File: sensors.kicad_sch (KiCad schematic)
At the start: 24 parts, among them J10 PH-2P, J11 PH-2P, J12 PH-2P, J13 PH-2P, J14 PH-2P, J15 PH-3P

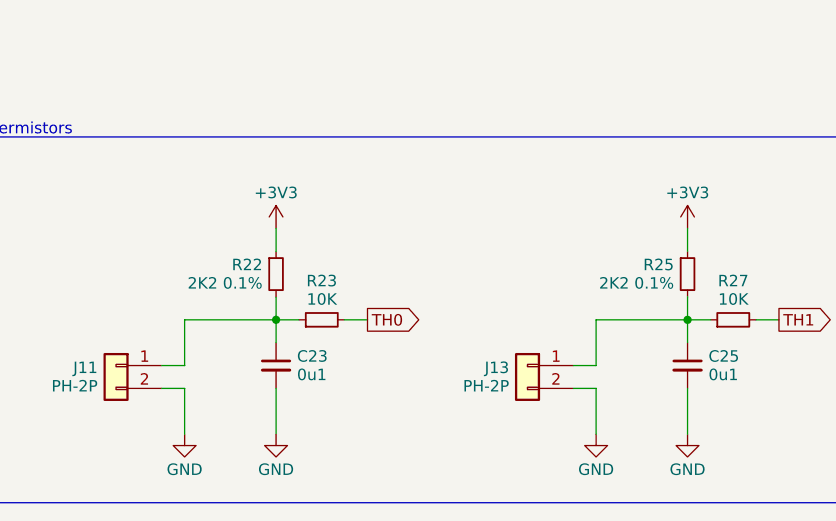
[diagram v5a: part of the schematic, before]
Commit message: Fix LCSC part for 74LVC2G17 (wrong package). List alternate parts in notes fields.
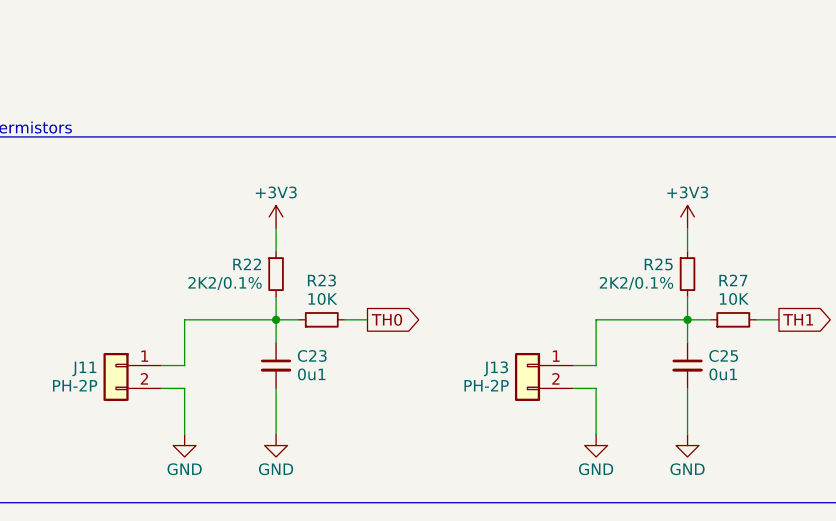
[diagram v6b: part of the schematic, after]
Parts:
- R22, R25: value 2K2 0.1% -> 2K2/0.1%
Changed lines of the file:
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@@
 			)
 		)
-		(property "Datasheet" "~"
+		(property "Datasheet" "https://www.smc-diodes.com/propdf/DSS12U%20THRU%20DSS125U%20N1873%20REV.A.pdf"
 			(at 48.26 93.98 90)
 			(effects
@@
 			)
 		)
-		(property "Value" "2K2 0.1%"
+		(property "Value" "2K2/0.1%"
 			(at 102.6414 143.264 0)
 			(effects
@@
 			)
 		)
-		(property "Value" "2K2 0.1%"
+		(property "Value" "2K2/0.1%"
 			(at 56.9214 143.264 0)
 			(effects
